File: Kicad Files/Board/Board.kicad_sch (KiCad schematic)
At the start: 28 parts, among them SW1 Boot, U1 RP2040, U2 W25Q128JVS, U3 SRV05-4, U4 XC6206PxxxMR, U5 X322512MSB4SI

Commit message: Modified Schematic
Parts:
- removed C13: 100nF, mechanical_keyboard:C_0402_1005Metric, symbol mechanical_keyboard:C_Small
- removed U3: SRV05-4, mechanical_keyboard:SOT-23-6, symbol mechanical_keyboard:SRV05-4
- added D1: 1N5819WS, mechanical_keyboard:D_SOD-323, symbol mechanical_keyboard:1N5819WS
- added J1: CSP-USC16-TR, mechanical_keyboard:USB_C_Receptacle_HRO_TYPE-C-31-M-12, symbol mechanical_keyboard:CSP-USC16-TR
- added R6, R7: 5k1, mechanical_keyboard:R_0402_1005Metric, symbol Device:R_Small_US
- added U3: USBLC6-2SC6, mechanical_keyboard:SOT-23-6, symbol mechanical_keyboard:USBLC6-2SC6
- C7: value 10uF -> 100nF; LCSC Part # C15525 -> C1525
- U2: footprint mechanical_keyboard:SOIC-8_5.23x5.23mm_P1.27mm -> Package_SO:SOIC-8_5.23x5.23mm_P1.27mm
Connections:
- net +3.3V: now also C1.2, C10.2, C11.2, C15.2, C7.2, C8.2, C9.2, U1.1 (IOVDD), U1.10 (IOVDD), U1.22 (IOVDD), U1.33 (IOVDD), U1.42 (IOVDD), U1.43 (ADC_AVDD), U1.44 (VREG_VIN), U1.48 (USB_VDD), U1.49 (IOVDD); no longer C1.1, C10.1, C11.1, C7.1, C9.1
- net +5V: now also D1.1 (K)
- net GND: now also C1.1, C10.1, C11.1, C12.1, C14.1, C15.1, C4.1, C5.1, C6.1, C7.1, C8.1, C9.1, U5.2, U5.4, J1.A1 (GND_A), J1.A12 (GND_A), J1.B1 (GND_B), J1.B12 (GND_B), J1.S1 (SHELL_GND), J1.S2 (SHELL_GND), J1.S3 (SHELL_GND), J1.S4 (SHELL_GND), R6.1, R7.1, U3.2 (GND); no longer C1.2, C7.2
- net at U1.23 (DVDD): now also U1.45 (VREG_VOUT), U1.50 (DVDD); no longer C15.2
- net D+: now reaches R2.2
- net D+: now also U3.6 (I/O1)
- net D-: now reaches R3.2
- net D-: now also U3.4 (I/O2)
- removed net +1V1: C15.1, C8.2, U1.50 (DVDD)
- net COl13 renamed COL13
- net COl14 renamed COL14
- net COl15 renamed COL15
- net COl16 renamed COL16
- net COl17 renamed COL17
- new net: J1.A5 (CC1), R7.2
- new net: J1.A7 (DN1), J1.B7 (DN2), U3.1 (I/O1)
- new net: J1.A6 (DP1), J1.B6 (DP2), U3.3 (I/O2)
- new net: D1.2 (A), J1.A4 (VBUS_A), J1.A9 (VBUS_A), J1.B4 (VBUS_B), J1.B9 (VBUS_B), U3.5 (VBUS)
- new net: J1.B5 (CC2), R6.2
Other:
- note added: "Decoupling Capacitors"
- note added: "USB"
- moved on the sheet: C16, C17, C2, C3, R5, U2, U4, U5

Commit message: Matrix Left
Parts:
- U1: footprint mechanical_keyboard:IC57_RP2040 -> IC57_RP2040
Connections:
- net D+: now also R3.2, U3.4 (I/O2); no longer R2.2, U3.6 (I/O1)
- net D-: now also R2.2, U3.6 (I/O1); no longer R3.2, U3.4 (I/O2)
- net at R2.1: now also U1.46 (USB_DM); no longer U1.47 (USB_DP)
- net at R3.1: now also U1.47 (USB_DP); no longer U1.46 (USB_DM)
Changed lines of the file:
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@@
 	(wire
 		(pts
-			(xy 140.97 57.15) (xy 151.13 57.15)
-		)
-		(stroke
-			(width 0)
-			(type default)
-		)
-	)
-	(wire
-		(pts
 			(xy 34.29 38.1) (xy 34.29 40.64)
 		)
@@
 	(wire
 		(pts
+			(xy 140.97 57.15) (xy 151.13 57.15)
+		)
+		(stroke
+			(width 0)
+			(type default)
+		)
+	)
+	(wire
+		(pts
 			(xy 52.07 85.09) (xy 80.01 85.09)
 		)
@@
 	(wire
 		(pts
-			(xy 157.48 90.17) (xy 157.48 88.9)
+			(xy 160.02 90.17) (xy 160.02 88.9)
 		)
 		(stroke
@@
 	(wire
 		(pts
-			(xy 140.97 54.61) (xy 143.51 54.61)
-		)
-		(stroke
-			(width 0)
-			(type default)
-		)
-	)
-	(wire
-		(pts
 			(xy 151.13 26.67) (xy 152.4 26.67)
 		)
@@
 	(wire
 		(pts
-			(xy 140.97 90.17) (xy 157.48 90.17)
+			(xy 140.97 90.17) (xy 160.02 90.17)
 		)
 		(stroke
@@
 	(wire
 		(pts
+			(xy 140.97 54.61) (xy 143.51 54.61)
+		)
+		(stroke
+			(width 0)
+			(type default)
+		)
+	)
+	(wire
+		(pts
 			(xy 78.74 176.53) (xy 86.36 176.53)
 		)
@@
 		)
 	)
-	(label "D-"
+	(label "D+"
 		(at 207.01 57.15 0)
 		(fields_autoplaced yes)
@@
 		)
 	)
-	(label "D+"
+	(label "D-"
 		(at 207.01 54.61 0)
 		(fields_autoplaced yes)
@@
 	(symbol
 		(lib_id "power:+3.3V")
-		(at 157.48 88.9 0)
+		(at 160.02 88.9 0)
 		(unit 1)
 		(exclude_from_sim no)
@@
 		(dnp no)
 		(property "Reference" "#PWR07"
-			(at 157.48 92.71 0)
+			(at 160.02 92.71 0)
 			(effects
 				(font
@@
 		)
 		(property "Value" "+3.3V"
-			(at 153.67 85.852 0)
+			(at 156.21 85.852 0)
 			(effects
 				(font
@@
 		)
 		(property "Footprint" ""
-			(at 157.48 88.9 0)
+			(at 160.02 88.9 0)
 			(effects
 				(font
@@
 		)
 		(property "Datasheet" ""
-			(at 157.48 88.9 0)
+			(at 160.02 88.9 0)
 			(effects
 				(font
@@
 		)
 		(property "Description" "Power symbol creates a global label with name \"+3.3V\""
-			(at 157.48 88.9 0)
+			(at 160.02 88.9 0)
 			(effects
 				(font
@@
 			)
 		)
-		(property "Footprint" "mechanical_keyboard:IC57_RP2040"
+		(property "Footprint" "IC57_RP2040"
 			(at 80.01 29.21 0)
 			(effects
@@
 			)
 		)
-		(property "Datasheet" "https://jlcpcb.com/api/file/downloadByFileSystemAccessId/8550723933012836352"
+		(property "Datasheet" "RP2040"
 			(at 80.01 29.21 0)
 			(effects

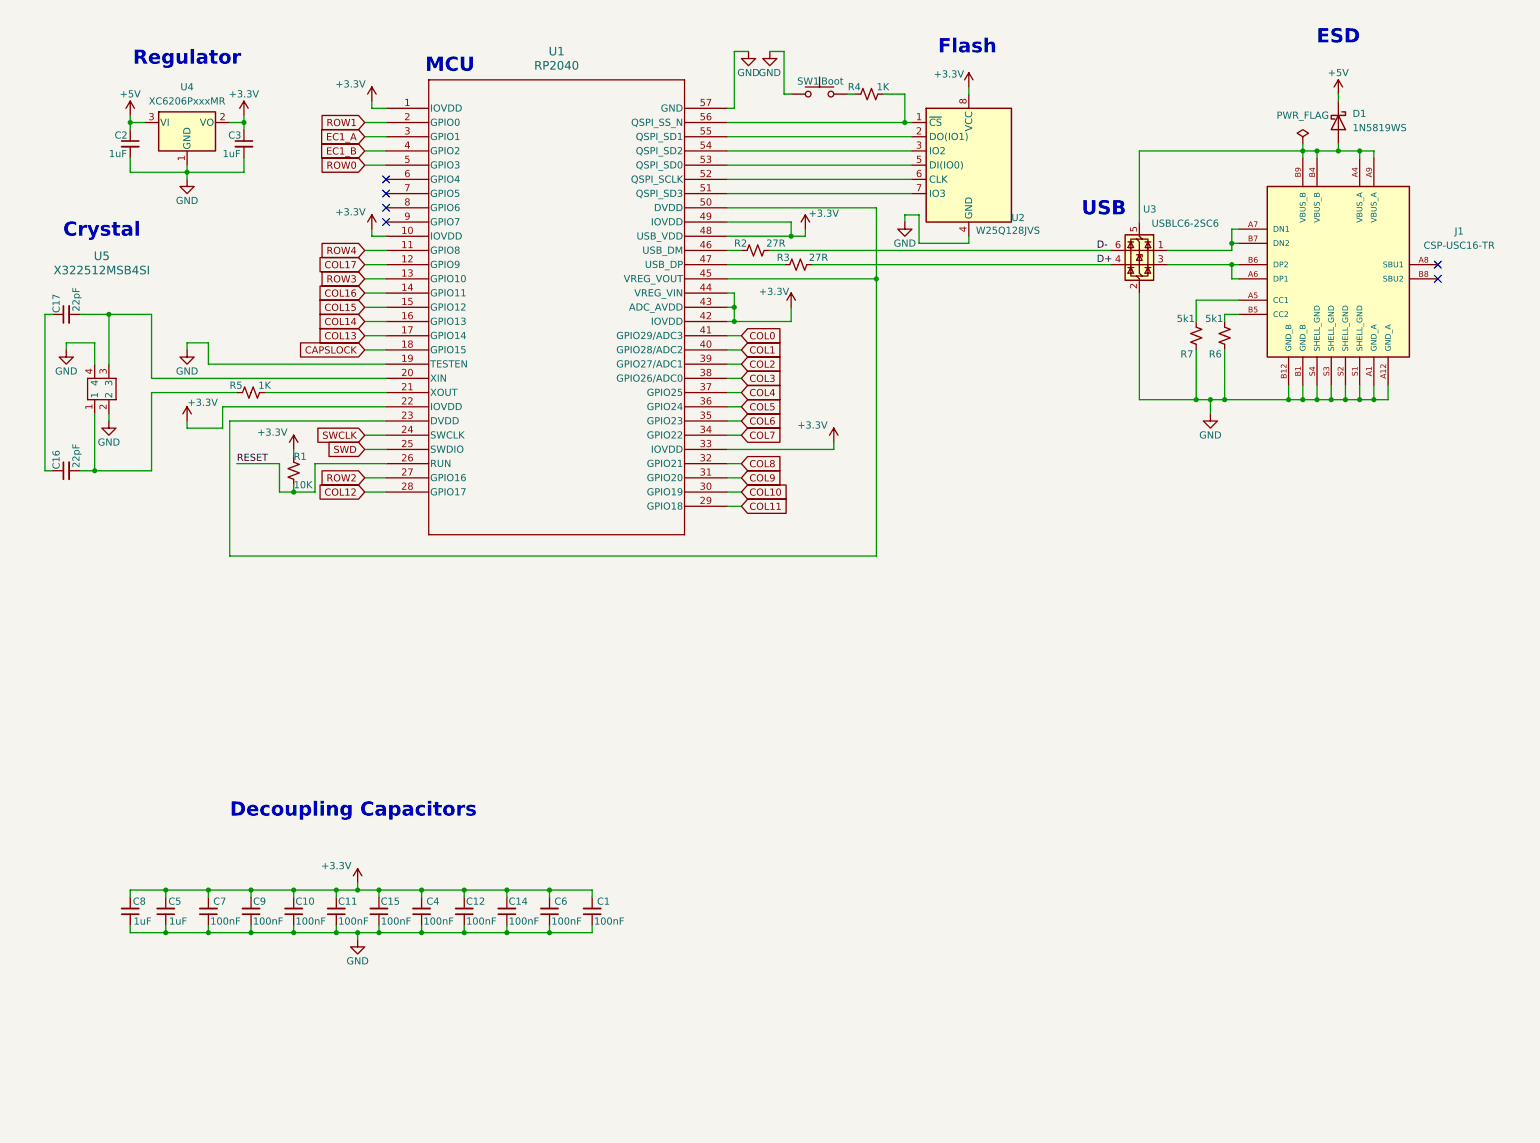
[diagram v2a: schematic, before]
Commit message: Schematic - Matrix Reduction Needed
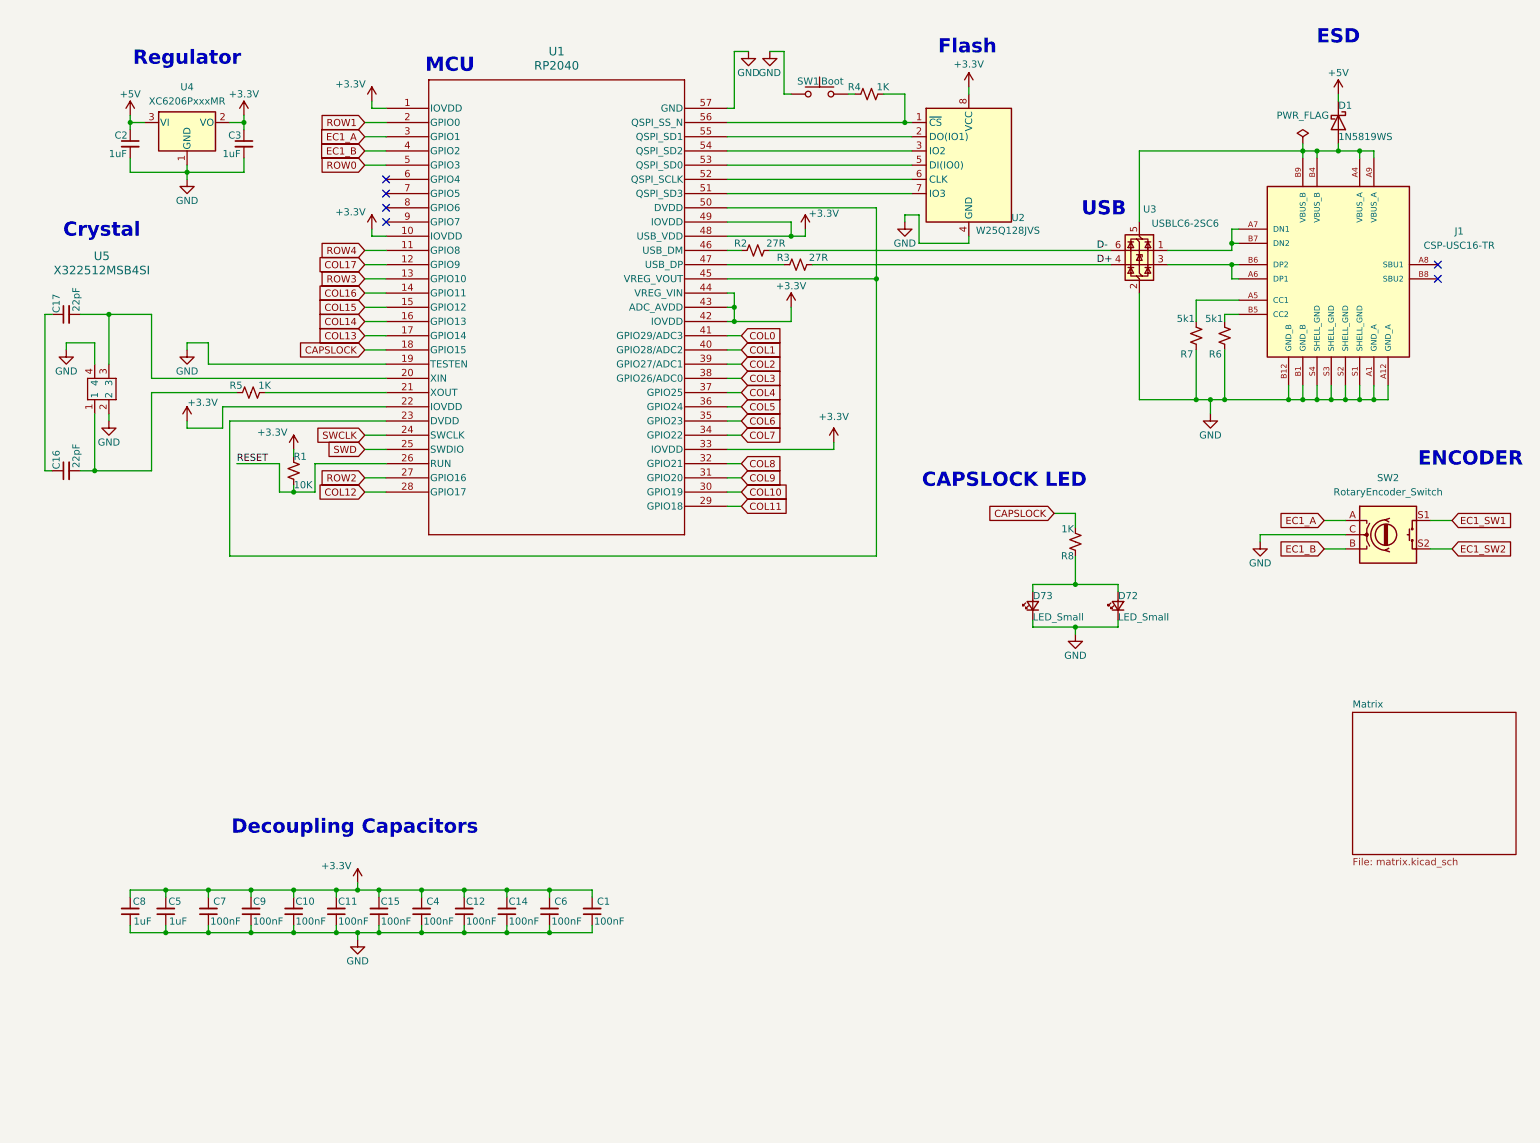
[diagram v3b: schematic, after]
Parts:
- added D72, D73: LED_Small, mechanical_keyboard:LED_0603_1608Metric, symbol mechanical_keyboard:LED_Small
- added R8: 1K, mechanical_keyboard:R_0402_1005Metric, symbol Device:R_Small_US
- added SW2: RotaryEncoder_Switch, symbol mechanical_keyboard:RotaryEncoder_Switch
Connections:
- net CAPSLOCK: now also R8.2
- net EC1_A: now also SW2.A
- net EC1_B: now also SW2.B
- net GND: now also D72.1 (K), D73.1 (K), SW2.C
- new net: D72.2 (A), D73.2 (A), R8.1
- new net EC1_SW1: SW2.S1
- new net EC1_SW2: SW2.S2
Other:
- added sheet Matrix (matrix.kicad_sch)
- note added: "CAPSLOCK LED"
- note added: "ENCODER"

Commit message: PCB Space
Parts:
- removed C1, C10, C11, C12, C14, C15, C4, C6, C7, C9: 100nF, mechanical_keyboard:C_0402_1005Metric, symbol mechanical_keyboard:C_Small
- removed C16, C17: 22pF, mechanical_keyboard:C_0402_1005Metric, symbol mechanical_keyboard:C_Small
- removed C2, C3, C5, C8: 1uF, mechanical_keyboard:C_0402_1005Metric, symbol mechanical_keyboard:C_Small
- removed D1: 1N5819WS, mechanical_keyboard:D_SOD-323, symbol mechanical_keyboard:1N5819WS
- removed J1: CSP-USC16-TR, mechanical_keyboard:USB_C_Receptacle_HRO_TYPE-C-31-M-12, symbol mechanical_keyboard:CSP-USC16-TR
- removed R1: 10K, mechanical_keyboard:R_0402_1005Metric, symbol Device:R_Small_US
- removed R2, R3: 27R, mechanical_keyboard:R_0402_1005Metric, symbol Device:R_Small_US
- removed R4, R5: 1K, mechanical_keyboard:R_0402_1005Metric, symbol Device:R_Small_US
- removed R6, R7: 5k1, mechanical_keyboard:R_0402_1005Metric, symbol Device:R_Small_US
- removed SW1: Boot, mechanical_keyboard:SW4_KMR221GLFS_CNK, symbol mechanical_keyboard:SW_Push
- removed SW2: RotaryEncoder_Switch, symbol mechanical_keyboard:RotaryEncoder_Switch
- removed U1: RP2040, IC57_RP2040, symbol mechanical_keyboard:RP2040
- removed U2: W25Q128JVS, Package_SO:SOIC-8_5.23x5.23mm_P1.27mm, symbol mechanical_keyboard:W25Q128JVS
- removed U3: USBLC6-2SC6, mechanical_keyboard:SOT-23-6, symbol mechanical_keyboard:USBLC6-2SC6
- removed U4: XC6206PxxxMR, mechanical_keyboard:SOT-23-3, symbol mechanical_keyboard:XC6206PxxxMR
- removed U5: X322512MSB4SI, SMD_2MSB4SI_YXC, symbol mechanical_keyboard:X322512MSB4SI
- added U1: RP2040-ZERO, mechanical_keyboard:MODULE_RP2040-ZERO, symbol mechanical_keyboard:RP2040-ZERO
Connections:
- no-connect marks 6 -> 0
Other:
- note added: "MATRIX"
- note removed: "Crystal"
- note removed: "Decoupling Capacitors"
- note removed: "ENCODER"
- note removed: "ESD"
- note removed: "Flash"
- note removed: "MCU"
- note removed: "Regulator"
- note removed: "USB"
- moved on the sheet: D72, D73, R8

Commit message: Routing Completed
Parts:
- removed D72, D73: LED_Small, mechanical_keyboard:LED_0603_1608Metric, symbol mechanical_keyboard:LED_Small
- removed R8: 1K, mechanical_keyboard:R_0402_1005Metric, symbol Device:R_Small_US
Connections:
- net ROW4: now reaches U1.1 (GP0)
- net COL10: now reaches U1.10 (GP9)
- net COL9: now reaches U1.11 (GP10)
- net COL8: now reaches U1.12 (GP11)
- net COL7: now reaches U1.13 (GP12)
- net COL6: now reaches U1.14 (GP13)
- net COL5: now reaches U1.15 (GP14)
- net COL4: now reaches U1.16 (GP15)
- net COL3: now reaches U1.17 (GP26)
- net COL2: now reaches U1.18 (GP27)
- net COL1: now reaches U1.19 (GP28)
- net ROW3: now reaches U1.2 (GP1)
- net COL0: now reaches U1.20 (GP29)
- net COL14: now reaches U1.3 (GP2)
- net ROW1: now reaches U1.4 (GP3)
- net ROW2: now reaches U1.5 (GP4)
- net ROW0: now reaches U1.6 (GP5)
- net COL13: now reaches U1.7 (GP6)
- net COL12: now reaches U1.8 (GP7)
- net COL11: now reaches U1.9 (GP8)
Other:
- note removed: "CAPSLOCK LED"
